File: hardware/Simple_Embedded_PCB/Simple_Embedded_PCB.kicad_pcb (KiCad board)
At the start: 2 copper layers, 62 parts, among them J1 USB_B_Micro, J2 SWD Connector, J3 Conn_01x09, J4 Conn_01x09, J5 Conn_01x09, J6 Conn_01x09, J7 5.5mm X 2.1mm Jack, Q1 AO3400A, Q2 AO3401A, U1 STM32F103C8Tx, U2 LMR16020PDDA, U3 AMS1117-3.3, X1 SG-8018CE 8.000000MHz

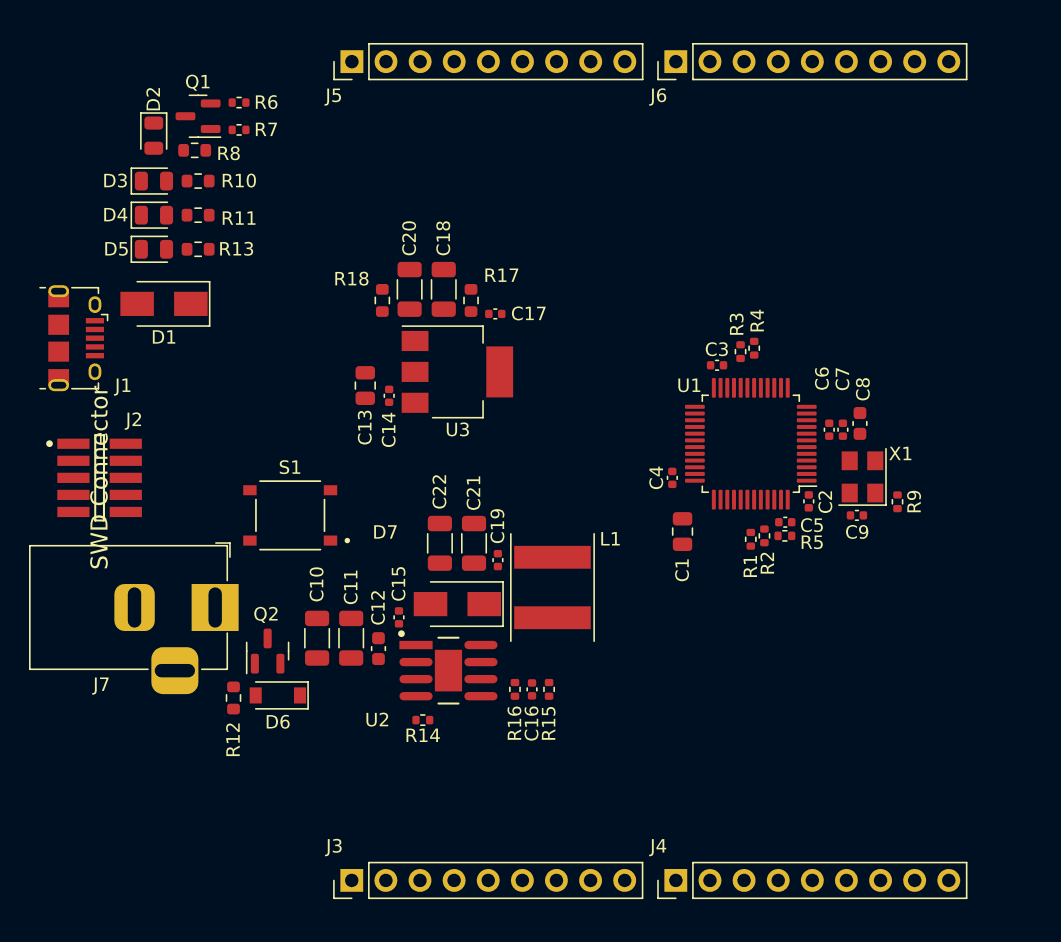
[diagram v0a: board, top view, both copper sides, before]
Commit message: Setup design rules and created proper board outline with mounting holes
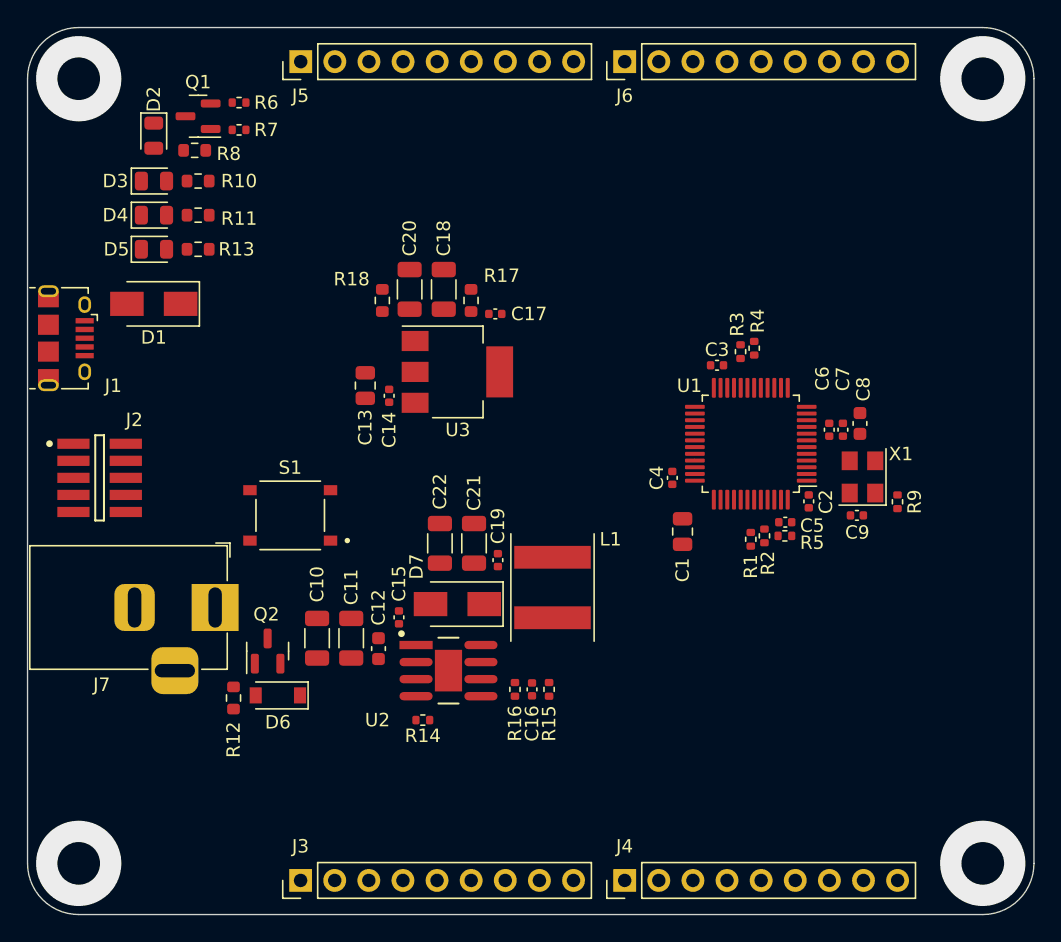
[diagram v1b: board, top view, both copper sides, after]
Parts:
- moved J3 3.81 mm to (43.2, 97.8)
- moved J4 3.81 mm to (67.3, 97.8)
- moved J6 3.81 mm to (67.3, 36.8)
- moved J5 3.81 mm to (43.2, 36.8)
- moved D1 0.76 mm to (32.3, 54.9)
- moved J1 0.76 mm to (25.7, 57.4)
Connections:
- net USB_DM renamed USB_N
- net USB_DP renamed USB_P
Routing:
- net GND: vias 0 -> 4
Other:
- board outline added: 74.9 x 66 mm
- copper layers 2 -> 4

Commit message: Routed all PCB traces, began routing power
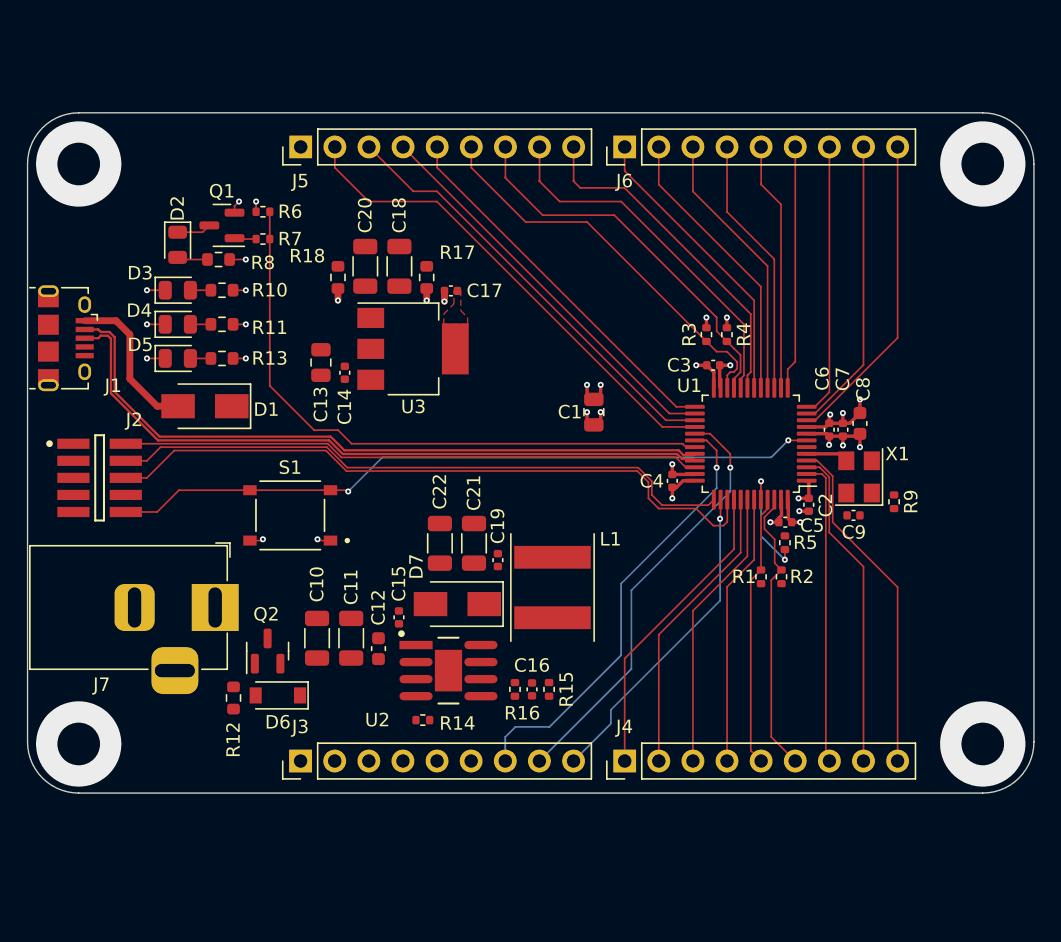
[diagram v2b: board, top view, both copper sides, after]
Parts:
- moved C1 11.1 mm to (65.0, 62.9)
- moved J3 8.89 mm to (43.2, 88.9)
- moved J4 8.89 mm to (67.3, 88.9)
- moved D1 8.52 mm to (36.1, 62.5)
- moved R6 8.32 mm to (40.4, 48.0)
- moved R7 8.32 mm to (40.4, 50.0)
- moved D2 8.32 mm to (34.0, 50.5)
- moved D3 8.32 mm to (34.1, 53.8)
- moved D4 8.32 mm to (34.1, 56.4)
- moved D5 8.32 mm to (34.1, 58.9)
- moved Q1 8.32 mm to (37.3, 49.0)
- moved R10 8.32 mm to (37.3, 53.8)
- moved R11 8.32 mm to (37.3, 56.4)
- moved R13 8.32 mm to (37.3, 58.9)
- moved R8 8.32 mm to (37.1, 51.6)
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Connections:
- J3 pad 7: TIM1_CH1 -> TIM1_CH2
- J3 pad 8: TIM1_CH2 -> TIM1_CH1
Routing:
- net NRST: track 0.00 -> 53.0 mm, vias 0 -> 2
- net USB_P: track 0.04 -> 51.8 mm
- net USB_N: track 0.04 -> 51.8 mm
- net SWO: track 0.00 -> 50.4 mm
- net SWCLK: track 0.00 -> 47.8 mm
- net Net-(R6-Pad1): track 0.00 -> 46.4 mm
- net SWDIO: track 0.00 -> 43.1 mm
- net SPI2_MOSI: track 0.00 -> 36.3 mm
- net TIM1_CH2: track 0.00 -> 33.1 mm, vias 0 -> 1
- net SPI2_MISO: track 0.00 -> 32.7 mm
- net TIM1_CH1: track 0.00 -> 32.0 mm, vias 0 -> 1
- net SPI2_SCK: track 0.00 -> 30.0 mm
- net I2C2_SDA: track 0.00 -> 29.7 mm
- net I2C2_SCL: track 0.00 -> 29.2 mm
- net GPIO_1: track 0.00 -> 28.1 mm
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- added copper zone on F.Cu, net +3.3V
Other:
- board size 74.9 x 66 mm -> 74.9 x 50.6 mm

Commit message: Finished layout, added step models and silkscreen
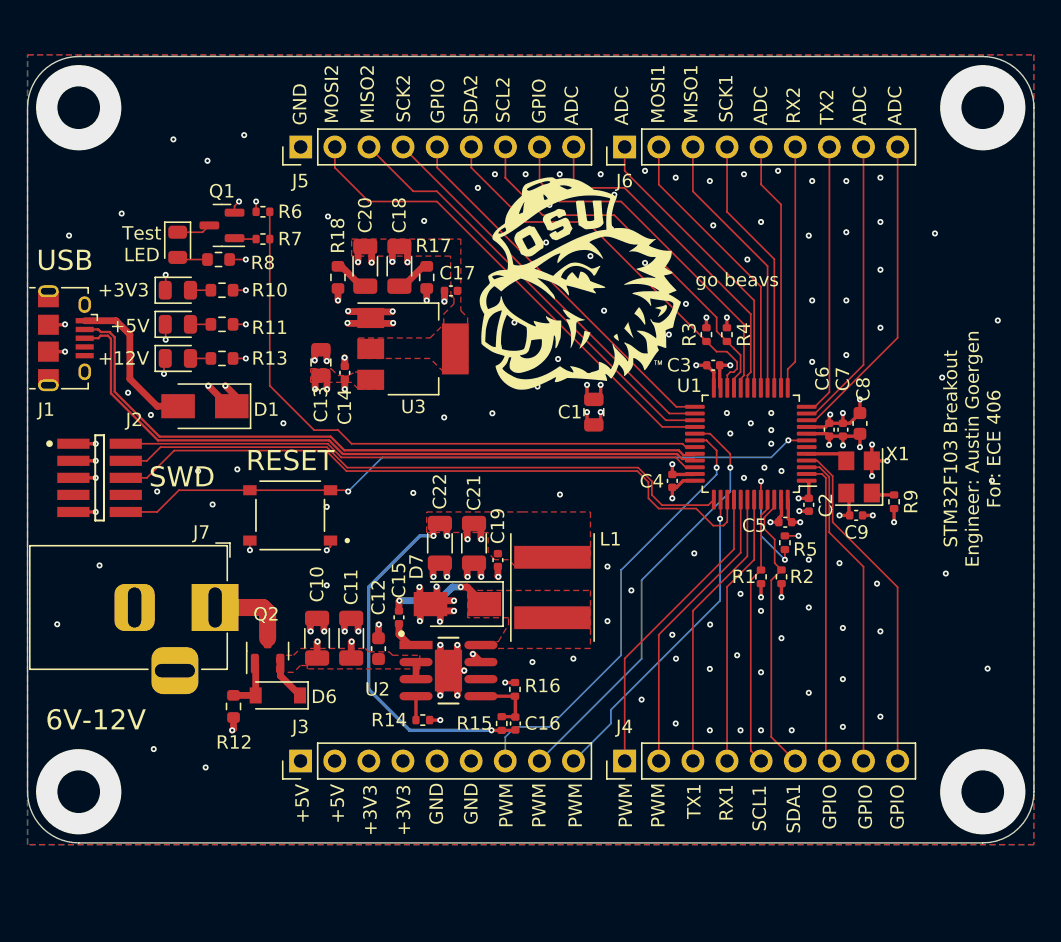
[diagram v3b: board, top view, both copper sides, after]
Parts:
- added G***: LOGO, LOGO, F.Cu at (64.0, 53.3)
- moved R15 4.35 mm to (58.2, 86.1), turned to -90 degrees
- moved C16 2.83 mm to (59.2, 86.1), turned to 90 degrees
- moved R12 0.63 mm to (38.2, 84.8)
- moved C9 0.20 mm to (84.6, 70.6)
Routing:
- net GND: track 26.4 -> 78.3 mm, vias 23 -> 174
- net +5V: track 0.95 -> 37.5 mm, vias 1 -> 11
- net +3.3V: track 22.8 -> 34.3 mm, vias 13 -> 22
- net Net-(C15-Pad2): track 0.00 -> 8.04 mm, vias 0 -> 2
- net +12V: track 0.95 -> 7.66 mm, vias 1 -> 3
- net /Power/Vin: track 0.00 -> 6.01 mm
- net Net-(C16-Pad2): track 0.00 -> 5.13 mm
- net Net-(D6-Pad2): track 0.00 -> 4.27 mm
- net Net-(C20-Pad2): track 0.00 -> 2.64 mm
- net Net-(C18-Pad2): track 0.00 -> 2.64 mm
- net Net-(C15-Pad1): track 0.00 -> 2.38 mm
- net Net-(R14-Pad2): track 0.00 -> 1.78 mm
- net Net-(R9-Pad2): track 0.00 -> 1.71 mm
- added copper zone on F.Cu, net +12V
- added copper zone on In2.Cu, net +12V
- added copper zone on In2.Cu, net +3.3V
- added copper zone on F.Cu, net +5V
- added copper zone on In2.Cu, net +5V
- added copper zone on B.Cu, net GND
- added copper zone on F.Cu, net GND
- added copper zone on In1.Cu, net GND
- added copper zone on In2.Cu, net GND
- added copper zone on F.Cu, net Net-(C15-Pad2)
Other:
- board size 74.9 x 50.6 mm -> 74.9 x 58.5 mm
- board text added: "+12V"
- board text added: "+3V3"
- board text added: "+5V"
- board text added: "6V-12V"
- board text added: "ADC"
- board text added: "GND"
- board text added: "GPIO"
- board text added: "MISO1"
- board text added: "MISO2"
- board text added: "MOSI1"
- board text added: "MOSI2"
- board text added: "PWM"
- board text added: "RESET"
- board text added: "RX1"
- board text added: "RX2"
- board text added: "SCK1"
- board text added: "SCK2"
- board text added: "SCL1"
- board text added: "SCL2"
- board text added: "SDA1"
- board text added: "SDA2"
- board text added: "STM32F103 Breakout Engineer: Austin Goergen For: ECE 406"
- board text added: "SWD"
- board text added: "TX1"
- board text added: "TX2"
- board text added: "Test LED"
- board text added: "USB"
- board text added: "go beavs"

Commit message: Added tooling holes and put JLCPCB order number on back of board, added kicad_prl file to git ignore
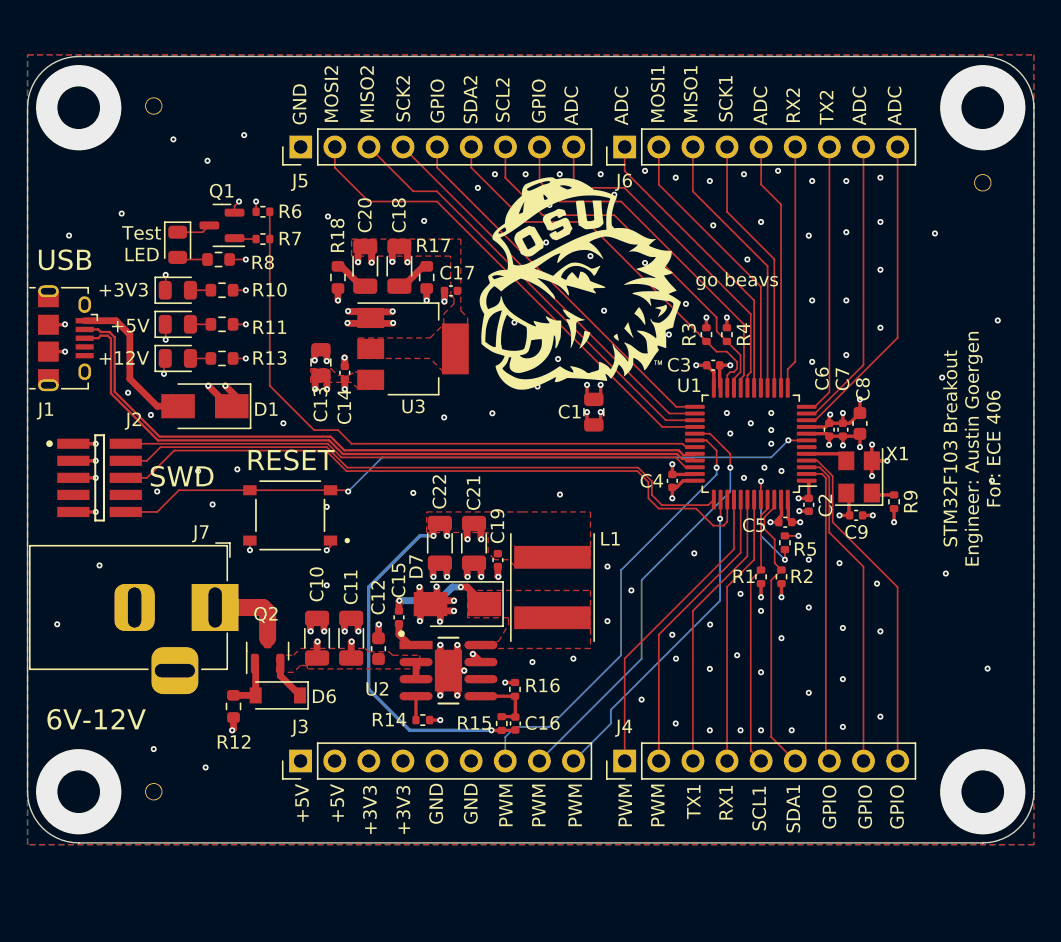
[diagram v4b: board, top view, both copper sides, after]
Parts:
- added H1: MountingHole, MySO:ToolingHole_JLCPCB, F.Cu at (32.3, 40.1)
- added H2: MountingHole, MySO:ToolingHole_JLCPCB, F.Cu at (94.0, 45.8)
- added H3: MountingHole, MySO:ToolingHole_JLCPCB, F.Cu at (32.3, 91.2)
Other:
- board text added: "JLCJLCJLCJLC"
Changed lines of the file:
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@@
   (net 62 "USB_P")
   (net 63 "USB_N")
+  (footprint "MySO:ToolingHole_JLCPCB" locked (layer "F.Cu")
+    (at 93.98 45.847)
+    (descr "Mounting Hole 2.1mm, no annular")
+    (tags "mounting hole 2.1mm no annular")
+    (property "Sheetfile" "Simple_Embedded_PCB.kicad_sch")
+    (property "Sheetname" "")
+    (attr exclude_from_pos_files)
+    (fp_text reference "H2" (at 0 -3.2) (layer "F.SilkS") hide
+      (effects (font (size 1 1) (thickness 0.15)))
+    )
+    (fp_text value "MountingHole" (at 0 3.2) (layer "F.Fab")
+      (effects (font (size 1 1) (thickness 0.15)))
+    )
+    (fp_text user "${REFERENCE}" (at 0 0) (layer "F.Fab")
+      (effects (font (size 1 1) (thickness 0.15)))
+    )
+    (fp_circle (center 0 0) (end 2.1 0) (layer "Cmts.User") (width 0.15) (fill none))
+    (fp_circle (center 0 0) (end 2.35 0) (layer "F.CrtYd") (width 0.05) (fill none))
+    (pad "" np_thru_hole circle locked (at 0 0) (size 1.3 1.3) (drill 1.152) (layers F&B.Cu *.Mask))
+  )
   (footprint "LOGO" (layer "F.Cu")
     (at 64.008 53.34)
@@
     )
   )
+  (footprint "MySO:ToolingHole_JLCPCB" locked (layer "F.Cu")
+    (at 32.258 40.132)
+    (descr "Mounting Hole 2.1mm, no annular")
+    (tags "mounting hole 2.1mm no annular")
+    (property "Sheetfile" "Simple_Embedded_PCB.kicad_sch")
+    (property "Sheetname" "")
+    (attr exclude_from_pos_files)
+    (fp_text reference "H1" (at 0 -3.2) (layer "F.SilkS") hide
+      (effects (font (size 1 1) (thickness 0.15)))
+    )
+    (fp_text value "MountingHole" (at 0 3.2) (layer "F.Fab")
+      (effects (font (size 1 1) (thickness 0.15)))
+    )
+    (fp_text user "${REFERENCE}" (at 0 0) (layer "F.Fab")
+      (effects (font (size 1 1) (thickness 0.15)))
+    )
+    (fp_circle (center 0 0) (end 2.1 0) (layer "Cmts.User") (width 0.15) (fill none))
+    (fp_circle (center 0 0) (end 2.35 0) (layer "F.CrtYd") (width 0.05) (fill none))
+    (pad "" np_thru_hole circle locked (at 0 0) (size 1.3 1.3) (drill 1.152) (layers F&B.Cu *.Mask))
+  )
   (footprint "Connector_PinHeader_2.54mm:PinHeader_1x09_P2.54mm_Vertical" (layer "F.Cu")
     (at 67.32 88.9 90)
@@
     )
   )
+  (footprint "MySO:ToolingHole_JLCPCB" locked (layer "F.Cu")
+    (at 32.258 91.186)
+    (descr "Mounting Hole 2.1mm, no annular")
+    (tags "mounting hole 2.1mm no annular")
+    (property "Sheetfile" "Simple_Embedded_PCB.kicad_sch")
+    (property "Sheetname" "")
+    (attr exclude_from_pos_files)
+    (fp_text reference "H3" (at 0 -3.2) (layer "F.SilkS") hide
+      (effects (font (size 1 1) (thickness 0.15)))
+    )
+    (fp_text value "MountingHole" (at 0 3.2) (layer "F.Fab")
+      (effects (font (size 1 1) (thickness 0.15)))
+    )
+    (fp_text user "${REFERENCE}" (at 0 0) (layer "F.Fab")
+      (effects (font (size 1 1) (thickness 0.15)))
+    )
+    (fp_circle (center 0 0) (end 2.1 0) (layer "Cmts.User") (width 0.15) (fill none))
+    (fp_circle (center 0 0) (end 2.35 0) (layer "F.CrtYd") (width 0.05) (fill none))
+    (pad "" np_thru_hole circle locked (at 0 0) (size 1.3 1.3) (drill 1.152) (layers F&B.Cu *.Mask))
+  )
   (footprint "Resistor_SMD:R_0402_1005Metric" (layer "F.Cu")
     (at 77.47 75.186 90)
@@
   (gr_line (start 93.98 94.996) (end 26.67 94.996) (layer "Edge.Cuts") (width 0.1))
   (gr_line (start 97.79 40.259) (end 97.79 91.186) (layer "Edge.Cuts") (width 0.1))
+  (gr_text "JLCJLCJLCJLC" (at 95.758 82.55 90) (layer "B.SilkS")
+    (effects (font (size 1 1) (thickness 0.15)) (justify mirror))
+  )
   (gr_text "go beavs" (at 75.692 53.086) (layer "F.SilkS")
     (effects (font (size 1 1) (thickness 0.153)))
